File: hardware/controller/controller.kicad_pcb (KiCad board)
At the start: 4 copper layers, 30 x 30 mm, 63 parts, among them J1 USB-C, J10 BTB 40P header, J11 BTB 40P header, J2 Qwiic, J3 Qwiic, Q1 AO3401A, SW1 BTN1, SW2 BTN2, SW3 BOOTSEL, U1 RP2354B, U2 USBLC6-2SC6, U3 ME6211C33M5G, U4 74AHCT1G125, Y1 12MHz

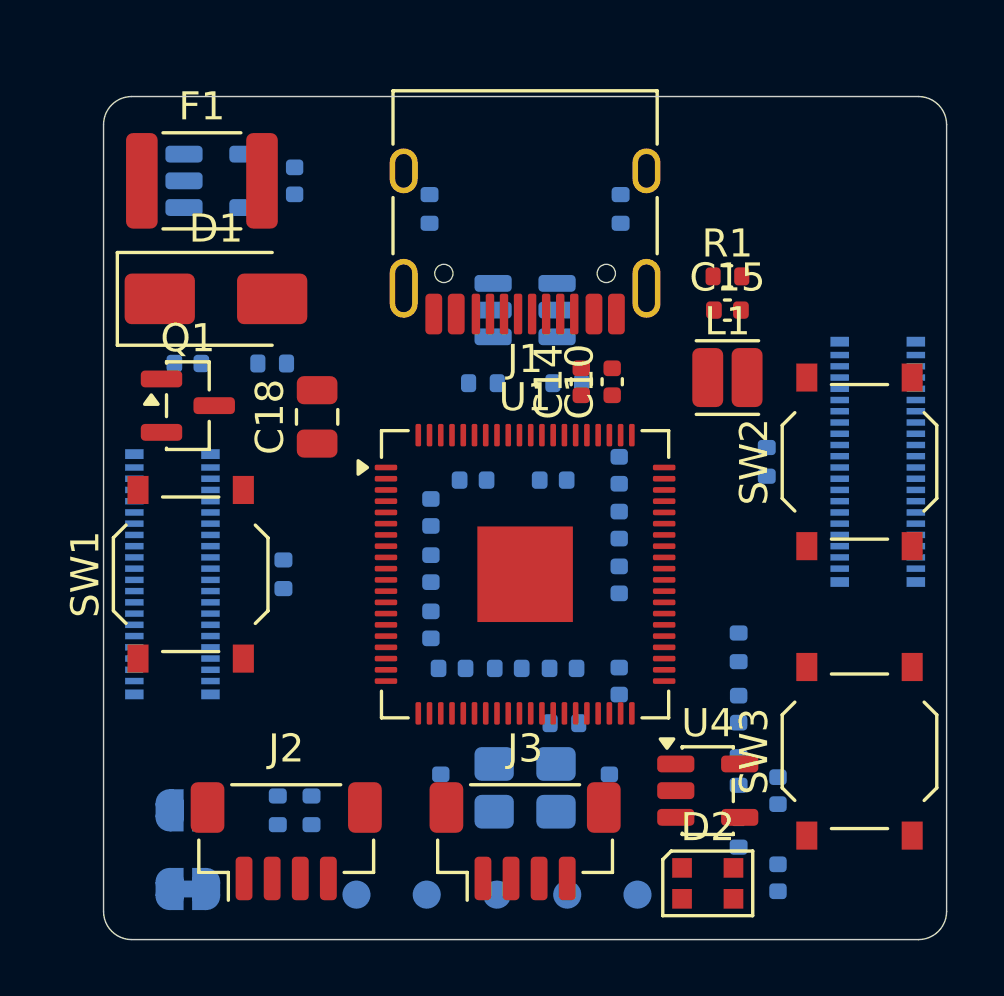
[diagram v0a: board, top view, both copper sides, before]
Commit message: Controller: route MCU supplies, crystal and core regulator
- Exposed-pad GND vias; every 3V3/1V1 pin vias to its underside 100 nF
  (3V3 vias land on the In2 plane), each cap with its own GND via.
- Crystal on the underside next to XIN/XOUT, with load caps and the
  1k XOUT resistor.
- Core regulator: short LX to L1 on top, PGND via, VIN cap over pin 64,
  1V1 cap by L1, AVDD RC moved to the underside behind L1.
- 1V1: In2 track from L1 to all four DVDD pins, ringed round the EP.
- USB-C 2 mm left of centre to make room for L1.
- Power net class clearance 0.15 -> 0.1 mm (JLCPCB standard), so the
  under-chip vias fit.

The PCB is the source from here; gen/pcbgen.py no longer recreates it.

Co-Authored-By: Claude Opus 5.5 <noreply@anthropic.com>
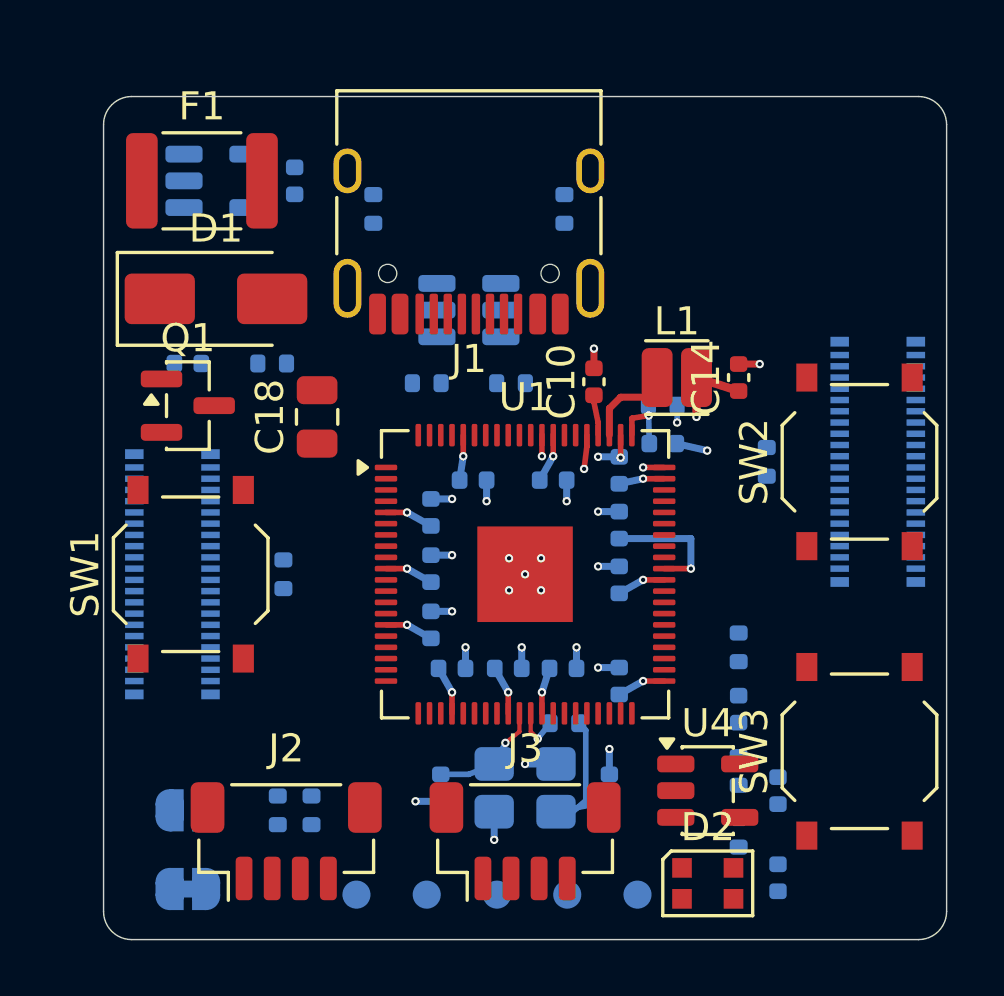
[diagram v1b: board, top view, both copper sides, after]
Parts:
- C15, R1: moved to B.Cu
- moved C14 5.60 mm to (107.6, 95.0)
- moved C15 5.28 mm to (104.9, 97.3)
- moved R1 5.14 mm to (104.9, 96.0), turned to 180 degrees
- moved J1 2.00 mm to (98.0, 88.7)
- moved R3 2.00 mm to (99.5, 95.2)
- moved R4 2.00 mm to (96.5, 95.2)
- moved R5 2.00 mm to (94.6, 89.0)
- moved R6 2.00 mm to (101.4, 89.0)
- moved U2 2.00 mm to (98.0, 92.6)
- moved L1 1.80 mm to (105.4, 95.0)
- moved C10 0.65 mm to (102.5, 95.2)
- turned C16 to -90 degrees
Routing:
- net /+1V1: track 0.00 -> 39.4 mm, vias 0 -> 5
- net /+3V3: track 0.00 -> 18.8 mm, vias 0 -> 12
- net /GND: track 0.00 -> 16.3 mm, vias 0 -> 25
- net /XTAL_OUT: track 0.00 -> 5.40 mm
- net /XIN: track 0.00 -> 4.11 mm, vias 0 -> 1
- net /VREG_AVDD: track 0.00 -> 2.56 mm, vias 0 -> 1
- net /VREG_LX: track 0.00 -> 2.52 mm
- net /XOUT: track 0.00 -> 1.71 mm, vias 0 -> 1

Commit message: Controller: route USB and the power path; TPD2E2U06 ESD
- ESD: USBLC6-2SC6 -> TPD2E2U06DRLR (SOT-553, C1972959) so it fits on
  the D+/D- path. Footprints re-linked to the regenerated symbols.
- USB: D- pads joined on top, D+ via-joined below; underside pair
  through the ESD and 27R series resistors back up to pins 66/67. CC1
  and CC2 5.1k to GND; VBUS lane above the pad row, then underside to F1.
- Power: F1 -> SS54 -> V5_IN -> AO3401A soft-start -> V5; LDO on V5_IN
  with its caps; V5 to connector A's inner and outer rows.
- In2 split: 3V3 island under the MCU, V5 ring around it feeding
  connector B (one via per pin group) and the LED corner.
- BTB headers (and the buttons over them) 1.3 mm inboard so the outer
  row can be fanned out with vias.

Co-Authored-By: Claude Opus 5.5 <noreply@anthropic.com>
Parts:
- U2: value USBLC6-2SC6 -> TPD2E2U06; footprint Package_TO_SOT_SMD:SOT-23-6 -> Package_TO_SOT_SMD:SOT-553
- moved R5 9.75 mm to (103.3, 93.4), turned to 0 degrees
- moved R6 7.91 mm to (96.2, 95.0), turned to -90 degrees
- moved C19 5.50 mm to (86.3, 88.0)
- moved C21 5.50 mm to (91.8, 88.0)
- moved R4 4.37 mm to (100.6, 96.7), turned to -90 degrees
- moved U2 2.91 mm to (99.9, 94.8)
- moved R3 2.45 mm to (102.0, 95.2), turned to -90 degrees
- moved R7 2.33 mm to (88.9, 93.5)
- moved J10 1.30 mm to (88.8, 102.0)
- moved J11 1.30 mm to (111.2, 98.0)
- moved SW1 0.65 mm to (88.8, 102.0)
- moved SW2 0.65 mm to (111.2, 98.0)
- turned C20 to 180 degrees
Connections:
- U2 pad 1: /USB_DP -> unconnected-(U2-NC-Pad1)
- U2 pad 2: /GND -> unconnected-(U2-NC-Pad2)
- U2 pad 3: /USB_DM -> /USB_DP
- U2 pad 4: /USB_DM -> /GND
- U2 pad 5: /VBUS -> /USB_DM
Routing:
- net /V5: track 0.00 -> 28.2 mm, vias 0 -> 9
- net /VBUS: track 0.00 -> 24.5 mm, vias 0 -> 2
- net /V5_IN: track 0.00 -> 22.0 mm, vias 0 -> 2
- net /GND: track 16.3 -> 25.8 mm, vias 25 -> 33
- net /+3V3: track 18.8 -> 26.6 mm, vias 12 -> 13
- net /USB_DM: track 0.00 -> 7.50 mm, vias 0 -> 1
- net /USB_DP: track 0.00 -> 6.51 mm, vias 0 -> 2
- net /CC1: track 0.00 -> 4.24 mm, vias 0 -> 1
- net /SS_GATE: track 0.00 -> 3.00 mm, vias 0 -> 1
- net /USB_DM_MCU: track 0.00 -> 2.88 mm, vias 0 -> 1
- net /VBUS_F: track 0.00 -> 1.93 mm
- net /USB_DP_MCU: track 0.00 -> 1.74 mm, vias 0 -> 1
- net /CC2: track 0.00 -> 1.03 mm, vias 0 -> 1
- added copper zone on In2.Cu, net /V5

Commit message: Controller: autoroute most signals with Freerouting (checkpoint)
GND/3V3 pad vias added; Freerouting 2.5.0 routed most of the BTB
fan-out and small signals (hand routing kept locked). 31 nets remain
unconnected around the BTB / button / MCU fan-out. Default vias
0.3/0.15 mm; Power tracks 0.25 mm.

Co-Authored-By: Claude Opus 5.5 <noreply@anthropic.com>
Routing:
- net /GND: track 25.8 -> 77.1 mm, vias 33 -> 45
- net /SDA: track 0.00 -> 34.3 mm, vias 0 -> 2
- net /+3V3: track 26.6 -> 59.8 mm, vias 13 -> 16
- net /LADDER: track 0.00 -> 28.2 mm, vias 0 -> 2
- net /SCL: track 0.00 -> 24.1 mm, vias 0 -> 2
- net /LED_DATA: track 0.00 -> 23.9 mm, vias 0 -> 1
- net /M8_AIN1: track 0.00 -> 22.7 mm, vias 0 -> 1
- net /M1_BIN2: track 0.00 -> 16.4 mm, vias 0 -> 1
- net /M7_BIN2: track 0.00 -> 15.7 mm, vias 0 -> 1
- net /M10_BIN2: track 0.00 -> 15.2 mm, vias 0 -> 1
- net /M6_BIN2: track 0.00 -> 15.0 mm, vias 0 -> 1
- net /QWIIC_3V3: track 0.00 -> 15.0 mm, vias 0 -> 1
- net /M6_AIN2: track 0.00 -> 14.9 mm, vias 0 -> 1
- net /M7_BIN1: track 0.00 -> 14.5 mm, vias 0 -> 5
- net /BOOT_R: track 0.00 -> 14.4 mm, vias 0 -> 1
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
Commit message: Controller: fully routed
- BTN1/BTN2 -> XUNPU TS-1088-AR02016 (C720477), stacked in the top-right
  corner with R11/R12 under them: the TS-1187A pads over the BTB headers
  blocked the connector fan-out.
- Connector B moved 2 mm down (stack still keyed by A's +2 mm offset);
  ladder/board-ID resistor column moved right, out of the M8 path.
- BTB corner contacts left unconnected (Hirose metal fittings).
- Routing: Freerouting 2.5.0 for the bulk, then a small grid router for
  the remaining nets and plane stitching. DRC: 0 unconnected, only
  silkscreen warnings and one harmless track stub left.

Co-Authored-By: Claude Opus 5.5 <noreply@anthropic.com>
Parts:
- R12: moved to F.Cu
- SW1, SW2: footprint Button_Switch_SMD:SW_Push_1P1T_XKB_TS-1187A -> Button_Switch_SMD:SW_SPST_TS-1088-xR020
- moved SW1 27.0 mm to (111.4, 87.2), turned to 0 degrees
- moved R11 23.9 mm to (111.4, 89.0), turned to 0 degrees
- moved SW2 7.25 mm to (111.4, 90.8), turned to 0 degrees
- moved R12 5.73 mm to (111.4, 93.0), turned to 180 degrees
- moved R10 5.04 mm to (112.4, 106.2)
- moved C22 4.97 mm to (112.4, 108.1)
- moved R13 4.97 mm to (112.4, 112.5)
- moved R14 4.97 mm to (112.4, 110.3)
- moved J11 2.00 mm to (111.2, 100.0)
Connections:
- J10 pad 1: /GND -> unconnected-(J10-Pin_1-Pad1)
- J10 pad 2: /GND -> unconnected-(J10-Pin_2-Pad2)
- J10 pad 39: /GND -> unconnected-(J10-Pin_39-Pad39)
- J10 pad 40: /GND -> unconnected-(J10-Pin_40-Pad40)
- J11 pad 1: /GND -> unconnected-(J11-Pin_1-Pad1)
- J11 pad 2: /GND -> unconnected-(J11-Pin_2-Pad2)
- J11 pad 39: /GND -> unconnected-(J11-Pin_39-Pad39)
- J11 pad 40: /GND -> unconnected-(J11-Pin_40-Pad40)
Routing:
- net /GND: track 77.1 -> 117.5 mm, vias 45 -> 41
- net /+3V3: track 59.8 -> 97.1 mm, vias 16 -> 18
- net /QSPI_SS: track 12.5 -> 46.1 mm, vias 2 -> 8
- net /BOARD_ID: track 7.69 -> 28.5 mm, vias 1 -> 4
- net /SCL: track 24.1 -> 42.2 mm, vias 2 -> 4
- net /SDA: track 34.3 -> 52.1 mm, vias 2 -> 7
- net /M8_BIN1: track 0.58 -> 15.3 mm, vias 0 -> 3
- net /LED_DIN: track 0.15 -> 14.7 mm, vias 0 -> 4
- net /M10_AIN2: track 1.33 -> 15.3 mm, vias 0 -> 5
- net /M7_AIN2: track 0.00 -> 13.8 mm, vias 0 -> 1
- net /CC1: track 4.97 -> 17.9 mm, vias 1 -> 2
- net /SWCLK: track 4.10 -> 16.7 mm, vias 0 -> 4
- net /M8_BIN2: track 0.63 -> 12.6 mm, vias 0 -> 3
- net /M9_BIN2: track 0.13 -> 11.2 mm, vias 0 -> 1
- net /CC2: track 2.81 -> 13.7 mm, vias 1 -> 2
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
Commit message: single_sh: routed single-board PCB; BOM scrub
New single-board versions of the circuit (controller + driver + IO variant
on one PCB, BTBs removed): single_sh and single_xh schematics from single()
in gen/build.py. single_sh also gets a routed board:

- 122 x 20 mm, 4 layers, 1.6 mm, all parts on top. In1 GND; In2 V5 with a
  3V3 island under the MCU (thin finger to the LDO); F/B signals.
- Along the board: USB-C + power | drivers M4-M1 | MCU | drivers M10-M5 |
  LED strip. Motor connectors J12 J11 | J15 J14 J13 so each bus leaves the
  MCU in pin order; misc connectors along the other long edge.
- Driver cells pre-routed (A1/A2 cross B1/B2 on In2 jumpers), core
  regulator copied from the controller, rest Freerouting 2.5.0 + a small
  grid router. V5 via clusters at the FET, ext-5V diode and strip fuse.
- DRC: 0 errors, 0 unconnected, schematic parity clean; 24 silkscreen
  warnings (footprint outlines).
- gen/pcbgen.py: build() split out of main(), per-board size/thickness,
  polygon zones, single_sh() placement (reproduces the routed board).

BOOTSEL on the single boards is now the TS-1088-AR02016 (C720477), same as
BTN1/BTN2; the stacked controller keeps its TS-1187A.

BOM scrub (all boards; numbers checked against the JLCPCB library):
- Every passive gets LCSC/MPN (PASSIVES in gen/build.py), basic where one
  exists. VM caps now 16 V (basic 2.2 uF is 6.3 V).
- Polyfuse C702823 (not in JLCPCB's library) -> C209721, same rating.
- Status LED C965555 (1 in stock) -> XL-2020RGBC-WS2812B C5349955, same
  pinout and footprint.
- J8 B3B-PH-K-S gets C131339.
- Solder jumpers and test pads excluded from BOM and placement files
  (schgen in_bom support; pcbgen follows the symbol).
- Schematics and *_bom.csv regenerated; controller PCB fields/attributes
  synced (layout unchanged).

Co-Authored-By: Claude Opus 5.5 <noreply@anthropic.com>
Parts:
- D2: value WS2812B-2020 -> XL-2020RGBC-WS2812B
